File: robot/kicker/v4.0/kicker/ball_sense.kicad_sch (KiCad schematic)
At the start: 3 parts, among them J16 Conn_01x10

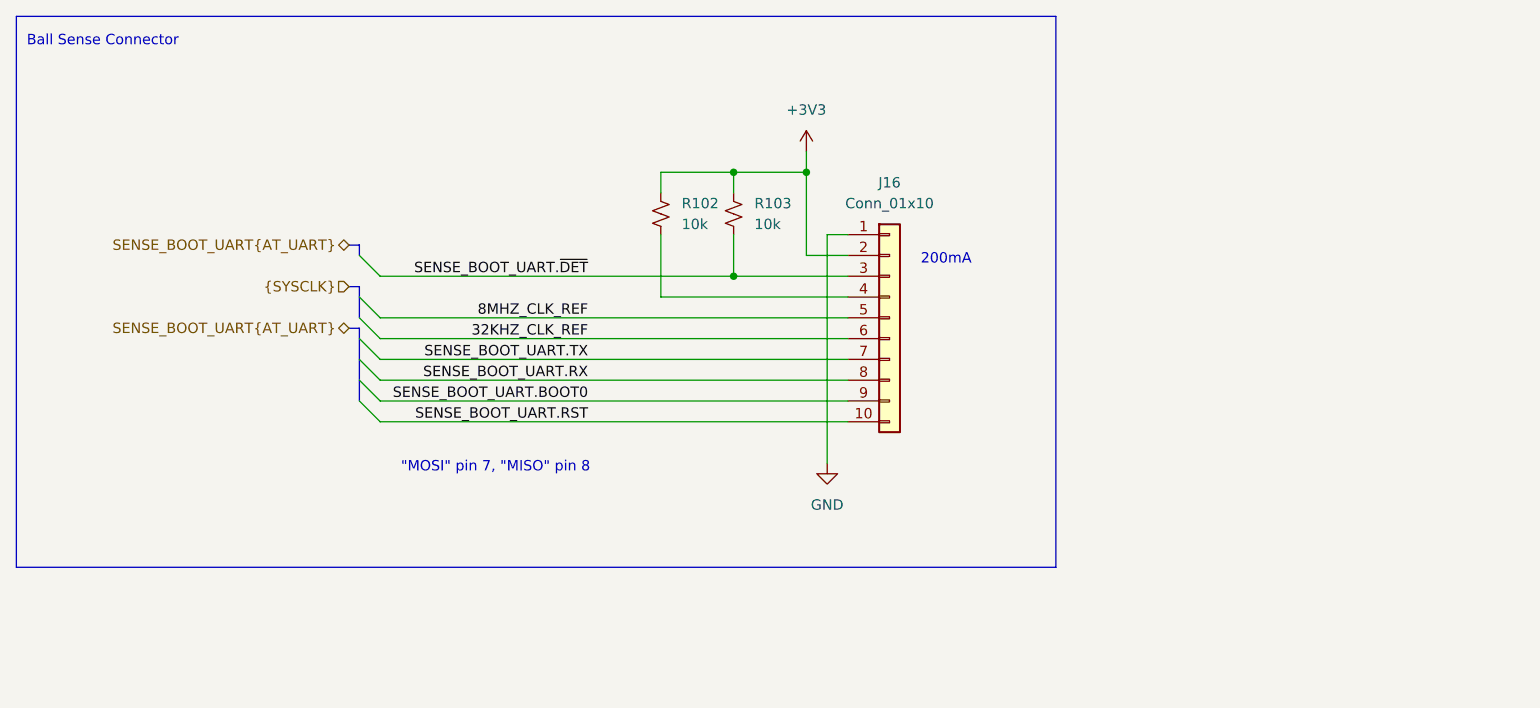
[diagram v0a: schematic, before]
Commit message: sch passing ERC
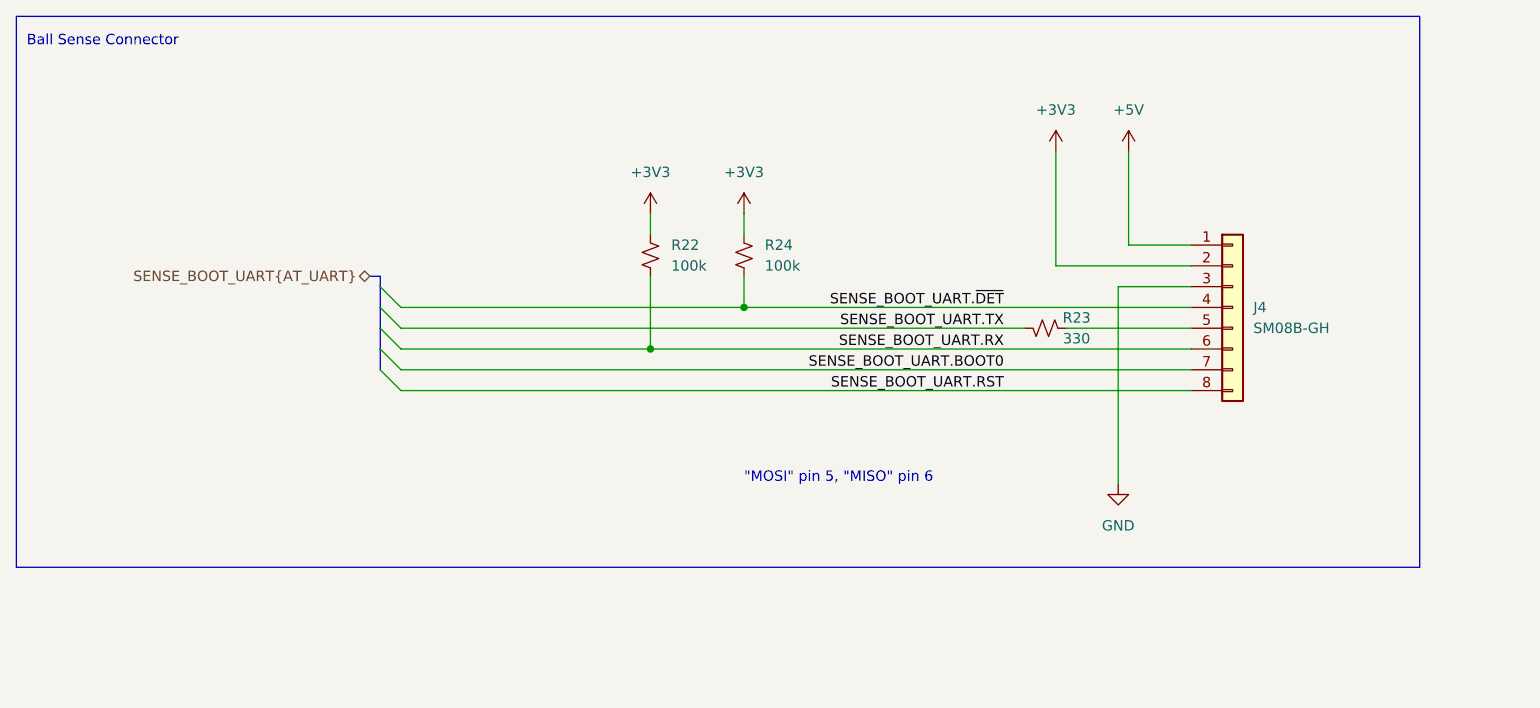
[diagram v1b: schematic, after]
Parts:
- removed J16: Conn_01x10, Connector_JST:JST_SH_SM10B-SRSS-TB_1x10-1MP_P1.00mm_Horizontal, symbol Connector_Generic:Conn_01x10
- removed R102, R103: 10k, Resistor_SMD:R_0402_1005Metric, symbol Device:R_Small_US
- added J4: SM08B-GH, Connector_JST:JST_GH_SM08B-GHS-TB_1x08-1MP_P1.25mm_Horizontal, symbol Connector_Generic:Conn_01x08
- added R22, R24: 100k, Resistor_SMD:R_0402_1005Metric, symbol Device:R_Small_US
- added R23: 330, Resistor_SMD:R_0402_1005Metric, symbol Device:R_Small_US
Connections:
- net +3V3: now also J4.2 (Pin_2), R22.1, R24.1
- net GND: now also J4.3 (Pin_3)
- net SENSE_BOOT_UART.BOOT0: now also J4.7 (Pin_7)
- net SENSE_BOOT_UART.RST: now also J4.8 (Pin_8)
- net SENSE_BOOT_UART.RX: now also J4.6 (Pin_6), R22.2
- net SENSE_BOOT_UART.TX: now also R23.2
- net SENSE_BOOT_UART.~{DET}: now also J4.4 (Pin_4), R24.2
- new net: J4.5 (Pin_5), R23.1
- new net +5V: J4.1 (Pin_1)
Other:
- note added: ""MOSI" pin 5, "MISO" pin 6"
- note removed: ""MOSI" pin 7, "MISO" pin 8"
- note removed: "200mA"

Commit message: initial board structure from dxf
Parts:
- renumbered J4 to J13, R22 to R78, R24 to R79, R23 to R80
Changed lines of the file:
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@@
 		(on_board yes)
 		(dnp no)
-		(property "Reference" "R23"
+		(property "Reference" "R80"
 			(at 148.59 55.88 90)
 			(effects
@@
 			(project "kicker"
 				(path "/7c007fad-bfbf-4e78-a837-1f8089552516/7a1ed07f-54d5-4760-ac90-4add0b6ea46f"
-					(reference "R23")
+					(reference "R80")
 					(unit 1)
 				)
@@
 		(dnp no)
 		(fields_autoplaced yes)
-		(property "Reference" "J4"
+		(property "Reference" "J13"
 			(at 170.18 54.6099 0)
 			(effects
@@
 			(project ""
 				(path "/7c007fad-bfbf-4e78-a837-1f8089552516/7a1ed07f-54d5-4760-ac90-4add0b6ea46f"
-					(reference "J4")
+					(reference "J13")
 					(unit 1)
 				)
@@
 		(dnp no)
 		(fields_autoplaced yes)
-		(property "Reference" "#PWR041"
+		(property "Reference" "#PWR0134"
 			(at 154.94 39.37 0)
 			(effects
@@
 			(project "kicker"
 				(path "/7c007fad-bfbf-4e78-a837-1f8089552516/7a1ed07f-54d5-4760-ac90-4add0b6ea46f"
-					(reference "#PWR041")
+					(reference "#PWR0134")
 					(unit 1)
 				)
@@
 		(dnp no)
 		(fields_autoplaced yes)
-		(property "Reference" "R22"
+		(property "Reference" "R78"
 			(at 99.06 46.9899 0)
 			(effects
@@
 			(project "kicker"
 				(path "/7c007fad-bfbf-4e78-a837-1f8089552516/7a1ed07f-54d5-4760-ac90-4add0b6ea46f"
-					(reference "R22")
+					(reference "R78")
 					(unit 1)
 				)
@@
 		(dnp no)
 		(fields_autoplaced yes)
-		(property "Reference" "#PWR042"
+		(property "Reference" "#PWR0133"
 			(at 146.05 39.37 0)
 			(effects
@@
 			(project "kicker"
 				(path "/7c007fad-bfbf-4e78-a837-1f8089552516/7a1ed07f-54d5-4760-ac90-4add0b6ea46f"
-					(reference "#PWR042")
+					(reference "#PWR0133")
 					(unit 1)
 				)
@@
 		(dnp no)
 		(fields_autoplaced yes)
-		(property "Reference" "R24"
+		(property "Reference" "R79"
 			(at 110.49 46.9899 0)
 			(effects
@@
 			(project "kicker"
 				(path "/7c007fad-bfbf-4e78-a837-1f8089552516/7a1ed07f-54d5-4760-ac90-4add0b6ea46f"
-					(reference "R24")
+					(reference "R79")
 					(unit 1)
 				)
@@
 		(dnp no)
 		(fields_autoplaced yes)
-		(property "Reference" "#PWR026"
+		(property "Reference" "#PWR0135"
 			(at 96.52 46.99 0)
 			(effects
@@
 			(project "kicker"
 				(path "/7c007fad-bfbf-4e78-a837-1f8089552516/7a1ed07f-54d5-4760-ac90-4add0b6ea46f"
-					(reference "#PWR026")
+					(reference "#PWR0135")
 					(unit 1)
 				)
@@
 		(dnp no)
 		(fields_autoplaced yes)
-		(property "Reference" "#PWR044"
+		(property "Reference" "#PWR0137"
 			(at 153.67 82.55 0)
 			(effects
@@
 			(project "kicker"
 				(path "/7c007fad-bfbf-4e78-a837-1f8089552516/7a1ed07f-54d5-4760-ac90-4add0b6ea46f"
-					(reference "#PWR044")
+					(reference "#PWR0137")
 					(unit 1)
 				)
@@
 		(dnp no)
 		(fields_autoplaced yes)
-		(property "Reference" "#PWR047"
+		(property "Reference" "#PWR0136"
 			(at 107.95 46.99 0)
 			(effects
@@
 			(project "kicker"
 				(path "/7c007fad-bfbf-4e78-a837-1f8089552516/7a1ed07f-54d5-4760-ac90-4add0b6ea46f"
-					(reference "#PWR047")
-					(unit 1)
-				)
+					(reference "#PWR0136")
+					(unit 1)
+				)

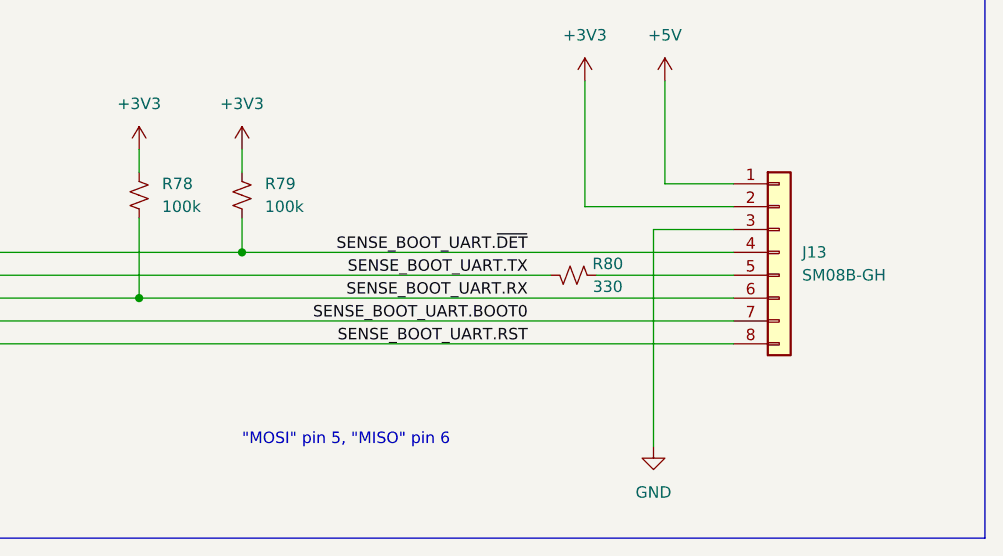
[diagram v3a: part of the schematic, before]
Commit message: Adjust for mechanical constraints and route board
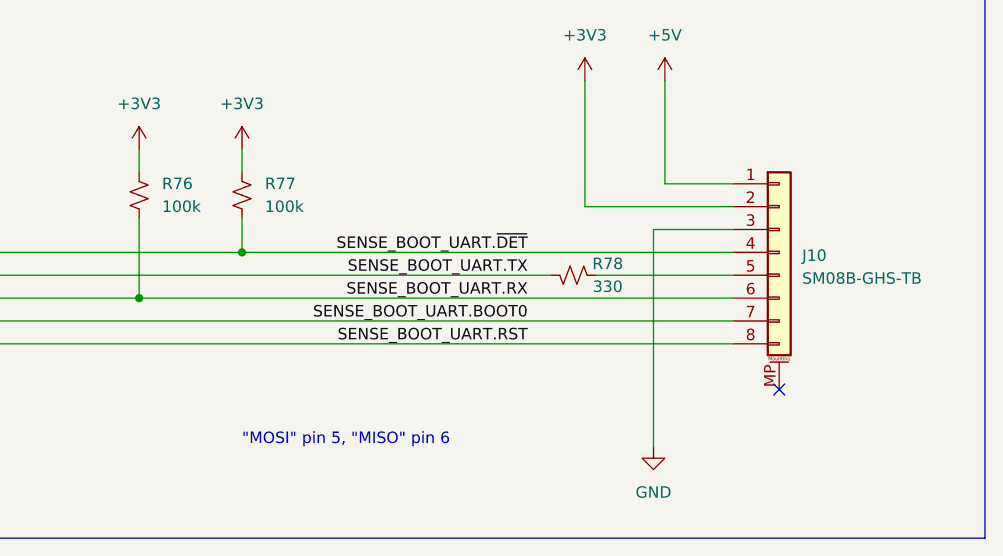
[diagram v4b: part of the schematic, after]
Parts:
- J10: renamed from J13; value SM08B-GH -> SM08B-GHS-TB; symbol Connector_Generic:Conn_01x08 -> Connector_Generic_MountingPin:Conn_01x08_MountingPin
- renumbered R78 to R76, R79 to R77, R80 to R78
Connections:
- no-connect marks 0 -> 1

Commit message: fixed old conenctors
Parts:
- removed J10: SM08B-GHS-TB, Connector_JST:JST_GH_SM08B-GHS-TB_1x08-1MP_P1.25mm_Horizontal, symbol Connector_Generic_MountingPin:Conn_01x08_MountingPin
- added J1: JST-SM10B-GHS, Connector_JST:JST_GH_SM10B-GHS-TB_1x10-1MP_P1.25mm_Horizontal, symbol Connector_Generic_MountingPin:Conn_01x10_MountingPin
- added R85: 330, Resistor_SMD:R_0402_1005Metric, symbol Device:R_Small_US
- added R86, R87: 100k, Resistor_SMD:R_0402_1005Metric, symbol Device:R_Small_US
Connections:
- net SENSE_BOOT_UART.~{DET} is gone; now on net SENSE_BOOT_UART.RX: R77.2
- net +3V3: now also J1.2 (Pin_2)
- net +5V: now also J1.1 (Pin_1)
- net GND: now also J1.3 (Pin_3), J1.4 (Pin_4), J1.MP (MountPin), R86.2, R87.2
- net SENSE_BOOT_UART.BOOT0: now also J1.5 (Pin_5), R87.1
- net SENSE_BOOT_UART.RST: now also J1.6 (Pin_6), R86.1
- net SENSE_BOOT_UART.RX: now also J1.8 (Pin_8); no longer R76.2
- net SENSE_BOOT_UART.TX: now also R78.1; no longer R78.2
- new net: J1.7 (Pin_7), R78.2
- new net: J1.10 (Pin_10), R85.2
- new net SENSE_BOOT_UART.CTS: J1.9 (Pin_9), R76.2
- new net SENSE_BOOT_UART.RTS: R85.1
- no-connect marks 1 -> 0
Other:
- note removed: ""MOSI" pin 5, "MISO" pin 6"

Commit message: kicker v4.0 prod files
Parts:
- J1: LCSC (none) -> C2683602
- R76, R77, R86, R87: LCSC (none) -> C60491
- R78, R85: LCSC (none) -> C105875
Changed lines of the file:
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@@
+			)
+		)
+		(property "LCSC" "C105875"
+			(at 137.16 57.15 0)
+			(effects
+				(font
+					(size 1.27 1.27)
+				)
+				(hide yes)
 			)
 		)
@@
 			)
 		)
+		(property "LCSC" "C60491"
+			(at 92.71 74.9299 0)
+			(effects
+				(font
+					(size 1.27 1.27)
+				)
+				(hide yes)
+			)
+		)
 		(pin "1"
 		)
@@
 			)
 		)
+		(property "LCSC" "C60491"
+			(at 102.87 74.9299 0)
+			(effects
+				(font
+					(size 1.27 1.27)
+				)
+				(hide yes)
+			)
+		)
 		(pin "1"
 		)
@@
 			)
 		)
+		(property "LCSC" "C60491"
+			(at 113.03 43.1799 0)
+			(effects
+				(font
+					(size 1.27 1.27)
+				)
+				(hide yes)
+			)
+		)
 		(pin "1"
 		)
@@
 			)
 		)
+		(property "LCSC" "C105875"
+			(at 137.16 64.77 0)
+			(effects
+				(font
+					(size 1.27 1.27)
+				)
+				(hide yes)
+			)
+		)
 		(pin "1"
 		)
@@
 			)
 		)
+		(property "LCSC" "C2683602"
+			(at 161.29 36.83 0)
+			(effects
+				(font
+					(size 1.27 1.27)
+				)
+				(hide yes)
+			)
+		)
 		(pin "8"
 		)
@@
 			(effects
 				(font
+					(size 1.27 1.27)
+				)
+				(hide yes)
+			)
+		)
+		(property "LCSC" "C60491"
+			(at 123.19 43.1799 0)
+			(effects
+				(font
